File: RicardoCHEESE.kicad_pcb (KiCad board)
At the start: 4 copper layers, 54.7 x 68.3 mm, 143 parts, among them IC1 SiC437BED-T1-GE3, J1 RBUS, J2 USB_C_Receptacle_USB2.0, J3 Conn_Coaxial, J4 Conn_01x06_Pin, J5 Conn_01x06_Pin, J6 Conn_01x06_Pin, J7 Conn_01x06_Pin, J8 Conn_01x02_Male, U1 ESP32-S3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

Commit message: CHEESE routing finished V1
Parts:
- moved TP18 6.55 mm to (156.6, 97.4)
- moved C35 6.11 mm to (133.1, 97.2), turned to 180 degrees
- moved C9 4.71 mm to (124.9, 63.4), turned to 90 degrees
- moved C2 4.58 mm to (128.9, 63.4), turned to -90 degrees
- moved TP2 3.94 mm to (128.0, 65.9)
- moved C36 3.10 mm to (130.1, 94.8), turned to 90 degrees
- moved L2 1.91 mm to (126.2, 66.6), turned to 90 degrees
- moved TP9 1.46 mm to (139.9, 90.7)
- moved TP15 1.34 mm to (128.2, 97.8)
- moved Y1 1.05 mm to (126.9, 63.4), turned to 0 degrees
- moved C42 0.73 mm to (138.2, 94.2)
- moved R20 0.57 mm to (150.7, 102.7), turned to -90 degrees
- moved TP11 0.55 mm to (147.0, 121.3)
- moved R33 0.53 mm to (157.6, 107.7)
- moved R32 0.51 mm to (157.6, 109.7)
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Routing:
- net 5V_PWR: track 12.8 -> 109.4 mm, vias 0 -> 6
- net PA_EN: track 0.00 -> 70.1 mm, vias 0 -> 8
- net PHOTO0_TRIG: track 0.00 -> 62.8 mm, vias 0 -> 4
- net SEL2: track 0.00 -> 62.4 mm, vias 0 -> 2
- net PHOTO2_TRIG: track 0.00 -> 58.9 mm, vias 0 -> 2
- net CAMERA3_TRIG: track 0.00 -> 58.3 mm, vias 0 -> 4
- net CAMERA0_TRIG: track 0.00 -> 58.2 mm, vias 0 -> 2
- net SEL1: track 0.00 -> 54.1 mm, vias 0 -> 2
- net CAMERA2_TRIG: track 0.00 -> 52.5 mm, vias 0 -> 2
- net CAMERA1_TRIG: track 0.00 -> 52.1 mm, vias 0 -> 2
- net PHOTO3_TRIG: track 0.00 -> 50.3 mm, vias 0 -> 4
- net PHOTO1_TRIG: track 0.00 -> 44.3 mm, vias 0 -> 4
- net PWR_GOOD: track 0.00 -> 43.1 mm, vias 0 -> 4
- net CS0: track 0.00 -> 40.7 mm, vias 0 -> 4
- net CS1: track 0.00 -> 40.5 mm, vias 0 -> 6
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- added copper zone on F.Cu, net +3.3V
- added copper zone on F.Cu, net +3.3VA
- added copper zone on F.Cu, net 5V_PWR
- added copper zone on F.Cu, net Net-(IC1-SW_1)
- added copper zone on F.Cu, net Net-(IC1-VIN_1)
- added copper zone on F.Cu, net Net-(U6-RF_IN)

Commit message: Finished routing
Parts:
- moved TP7 19.0 mm to (154.5, 81.4)
- moved J1 10.3 mm to (162.8, 68.2), turned to -90 degrees
- moved TP8 10.1 mm to (146.3, 88.6)
- moved TP10 5.99 mm to (151.8, 87.1)
- moved TP9 4.12 mm to (143.4, 88.5)
- moved R3 2.84 mm to (152.6, 66.7), turned to 90 degrees
- moved 12VLED1 0.91 mm to (151.2, 66.7), turned to 90 degrees
- moved TP5 0.67 mm to (120.1, 76.4)
- moved C14 0.66 mm to (119.3, 64.5), turned to -90 degrees
- moved TP3 0.50 mm to (122.3, 77.3)
- moved R12 0.45 mm to (120.0, 78.9)
- moved R14 0.27 mm to (149.7, 83.2), turned to 90 degrees
- moved TP4 0.19 mm to (123.4, 83.2)
- moved D2 0.10 mm to (123.3, 80.5), turned to -90 degrees
- turned C13 to 90 degrees
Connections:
- D2 pad 2: VBUS -> /Data-
- D2 pad 3: /Data- -> /Data+
- D2 pad 4: /Data+ -> VBUS
- U1 pad 30: unconnected-(U1-SPIHD/GPIO27-Pad30) -> /CAN_RX
- U1 pad 42: unconnected-(U1-GPIO37-Pad42) -> /CAN_TX
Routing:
- net VBUS: track 0.00 -> 54.4 mm, vias 0 -> 4
- net /Data+: track 0.00 -> 21.5 mm
- net /Data-: track 5.93 -> 19.8 mm
- net +3.3V: track 10.8 -> 23.9 mm, vias 6 -> 16
- net RBUS_uC_V: track 3.18 -> 14.6 mm
- net /Power/BBIN: track 0.00 -> 9.23 mm
- net GND: track 15.7 -> 24.7 mm, vias 6 -> 9
- net /CHIP_PU: track 5.71 -> 14.4 mm, vias 0 -> 2
- net /CAN_RX: track 0.00 -> 8.26 mm, vias 0 -> 2
- net /CAN+: track 10.4 -> 18.5 mm
- net /CAN-: track 9.73 -> 17.5 mm
- net /CAN_TX: track 0.00 -> 7.70 mm
- net /Power/BBOUT: track 0.00 -> 7.14 mm
- net /BOOT: track 3.55 -> 10.5 mm, vias 0 -> 2
- net +12V: track 0.25 -> 5.07 mm
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- added copper zone on F.Cu, net /Power/BBOUT
- added copper zone on F.Cu, net /Power/FBIn
- added copper zone on F.Cu, net Net-(C8-Pad2)

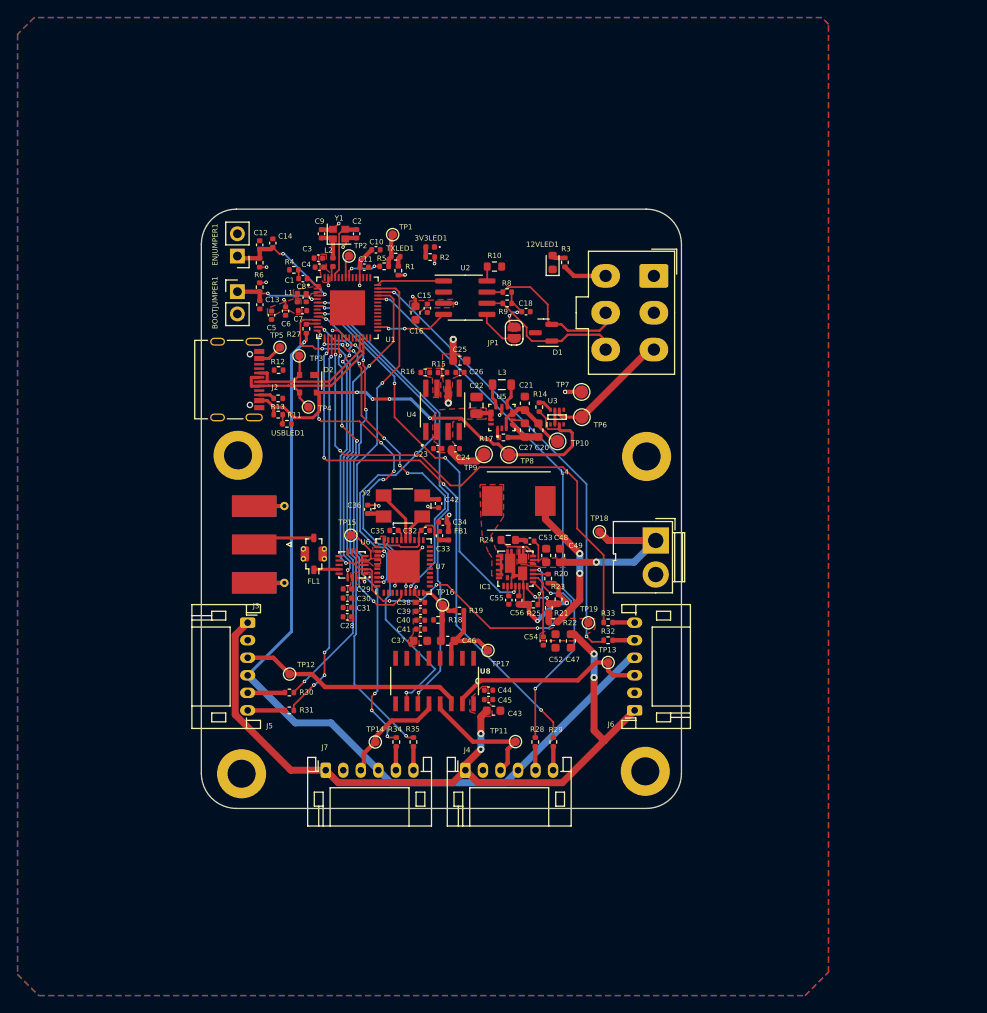
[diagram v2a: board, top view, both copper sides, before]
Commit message: radio side needs reviewing
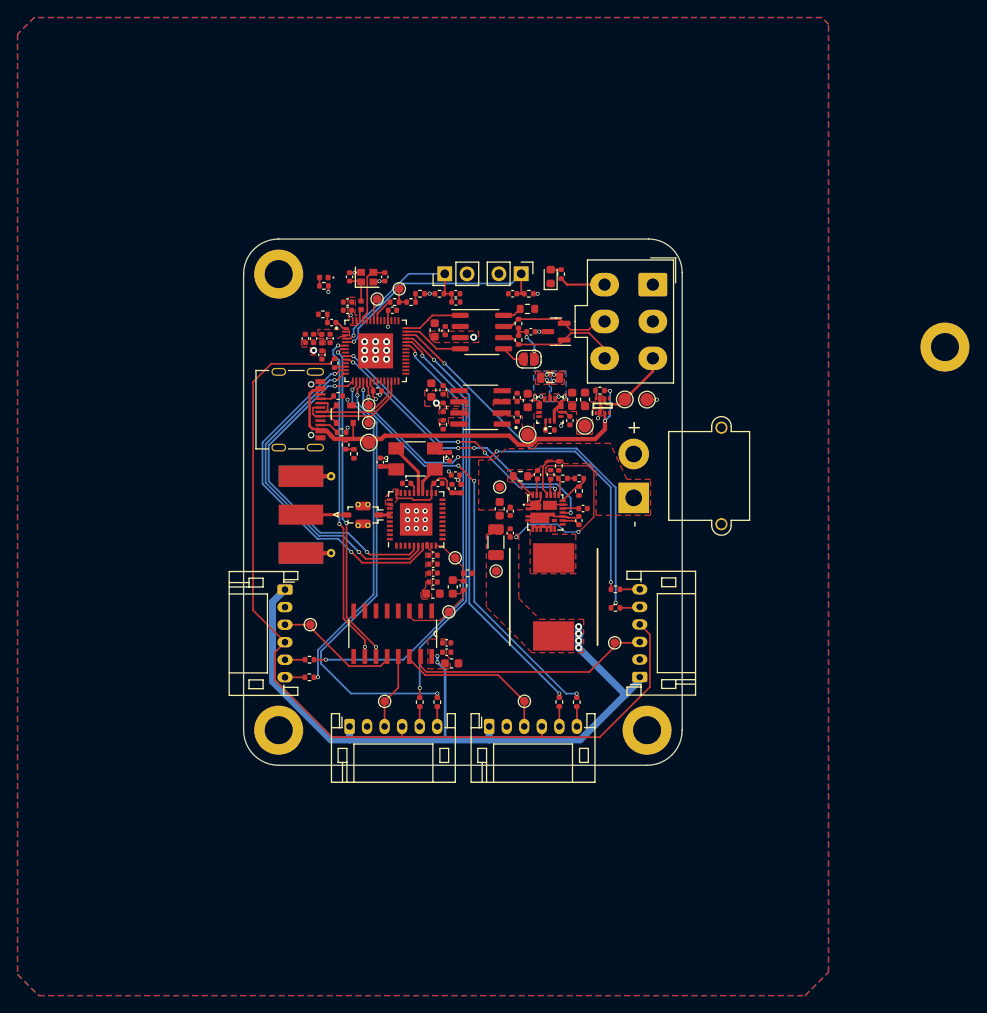
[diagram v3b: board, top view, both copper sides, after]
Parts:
- removed C28: 10u, Capacitor_SMD:C_0402_1005Metric
- removed C29, C30, C31: 100n, Capacitor_SMD:C_0402_1005Metric
- removed C47: 3u3, Capacitor_SMD:C_0603_1608Metric
- removed H2: MountingHole_Pad, MountingHole:MountingHole_3.2mm_M3_DIN965_Pad
- removed TP15, TP5: TestPoint, TestPoint:TestPoint_Pad_D1.0mm
- removed U6: SE5005L, fps:QFN300X300X100-16N
- added ?: , , F.Cu at (196.0, 76.3)
- C22: footprint Capacitor_SMD:C_0805_2012Metric -> Capacitor_SMD:C_0603_1608Metric
- C27: footprint Capacitor_SMD:C_0603_1608Metric -> Capacitor_SMD:C_0402_1005Metric
- C48: value 2u2 -> 10uF
- C49: value 1u5 -> 100nF; footprint Capacitor_SMD:C_0603_1608Metric -> Capacitor_SMD:C_0402_1005Metric
- C52: value 3u3 -> 47uF; footprint Capacitor_SMD:C_0603_1608Metric -> Capacitor_SMD:C_1206_3216Metric
- IC1: footprint fps:SiC437BEDT1GE3 -> iclr:SiC437BEDT1GE3
- J8: footprint Connector:JWT_A3963_1x02_P3.96mm_Vertical -> Connector_AMASS:AMASS_XT30PW-M_1x02_P2.50mm_Horizontal
- L4: value 11u -> 3.3uH; footprint Ricardo-CHEESE:IND_ASPI-0630HI-6R8M-T15 -> iclr:INDPM110100X540N
- R20: value 100k -> 51k
- R25: value 200k -> 100k
- U1: footprint fps:QFN40P700X700X90-57N -> iclr:QFN40P700X700X90-57N
- U3: footprint fps:SOTFL50P160X60-8N -> iclr:SOTFL50P160X60-8N
- U4: footprint fps:SOIC127P599X175-8N -> iclr:SOIC127P599X175-8N
- U5: footprint fps:CONV_MAX77827AEFD+T -> iclr:CONV_MAX77827AEFD+T
- U7: footprint Ricardo-CHEESE:RTC6705 -> iclr:RTC6705
- U8: footprint Ricardo-CHEESE:SOIC127P600X175-16N -> iclr:SOIC127P600X175-16N
- moved BOOTJUMPER1 32.4 mm to (147.7, 68.0), turned to -90 degrees
- moved R7 30.7 mm to (148.5, 70.2), turned to 180 degrees
- moved C13 28.8 mm to (146.7, 70.2), turned to 0 degrees
- moved ENJUMPER1 23.7 mm to (138.9, 68.0), turned to 90 degrees
- moved C12 23.0 mm to (140.2, 70.2), turned to 0 degrees
- moved C14 21.9 mm to (140.2, 71.2), turned to 180 degrees
- moved H1 21.2 mm to (120.0, 68.0)
- moved R6 20.8 mm to (138.3, 70.2), turned to 0 degrees
- moved R22 16.4 mm to (152.4, 91.3), turned to 0 degrees
- moved C10 16.1 mm to (131.2, 81.3)
- moved R25 16.1 mm to (151.9, 89.9), turned to 90 degrees
- moved TP8 16.0 mm to (130.3, 87.2), turned to -90 degrees
- moved R21 15.2 mm to (154.3, 91.3), turned to 0 degrees
- moved C52 13.2 mm to (144.8, 98.6), turned to -90 degrees
- moved C54 12.9 mm to (146.4, 97.5), turned to 90 degrees
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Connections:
- C56 pad 1: /Camera System/Camera Power Buck Converter/GNDA -> GND
- FL1 pad 1: /Camera System/RFOUT -> Net-(FL1-IN)
- IC1 pad 16: /Camera System/Camera Power Buck Converter/GNDA -> GND
- IC1 pad 19: PA_EN -> PWR_EN
- IC1 pad 25: /Camera System/Camera Power Buck Converter/GNDA -> GND
- R20 pad 2: /Camera System/Camera Power Buck Converter/GNDA -> GND
- R23 pad 2: /Camera System/Camera Power Buck Converter/GNDA -> GND
- R25 pad 1: /Camera System/Camera Power Buck Converter/GNDA -> GND
- U1 pad 10: PA_EN -> PWR_GOOD
- U1 pad 11: PA_PWR_DET -> unconnected-(U1-GPIO6/ADC1_CH5-Pad11)
- U1 pad 13: CS0 -> CS2
- U1 pad 15: CS2 -> CS0
- U1 pad 16: PHOTO0_TRIG -> PHOTO1_TRIG
- U1 pad 17: PHOTO1_TRIG -> PHOTO3_TRIG
- U1 pad 18: PHOTO2_TRIG -> PHOTO0_TRIG
- U1 pad 19: PHOTO3_TRIG -> PHOTO2_TRIG
- U1 pad 30: /CAN_RX -> unconnected-(U1-SPIHD/GPIO27-Pad30)
- U1 pad 37: unconnected-(U1-SPICLK_P/GPIO47-Pad37) -> CAMERA1_TRIG
- U1 pad 38: CAMERA0_TRIG -> CAMERA3_TRIG
- U1 pad 39: CAMERA1_TRIG -> CAMERA0_TRIG
- U1 pad 41: CAMERA3_TRIG -> /CAN_RX
- U1 pad 6: SEL1 -> SEL2
- U1 pad 7: SEL2 -> SEL1
- U1 pad 9: PWR_GOOD -> PWR_EN
- U3 pad 2: /Power/VoutDiode -> /Power/BBIN
- U3 pad 7: /Power/VoutDiode -> /Power/BBIN
- U7 pad 34: Net-(U6-RF_IN) -> Net-(FL1-IN)
- U7 pad 35: Net-(U6-RF_IN) -> Net-(FL1-IN)
- U8 pad 12: /Camera System/CAMERA3 -> /Camera System/CAMERA1
- U8 pad 13: /Camera System/CAMERA0 -> /Camera System/CAMERA3
- U8 pad 14: /Camera System/CAMERA1 -> /Camera System/CAMERA0
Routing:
- net PA_EN: track 70.1 -> 0.00 mm, vias 8 -> 0
- net PA_PWR_DET: track 36.5 -> 0.00 mm, vias 2 -> 0
- net PWR_EN: track 0.00 -> 31.0 mm, vias 0 -> 4
- net SEL2: track 62.8 -> 38.0 mm, vias 2 -> 3
- net Net-(IC1-VIN_1): track 18.8 -> 1.44 mm, vias 1 -> 0
- net SEL1: track 54.4 -> 37.5 mm, vias 2 -> 3
- net /BOOT: track 10.5 -> 27.0 mm, vias 2 -> 1
- net +3.3V: track 23.9 -> 9.09 mm, vias 16 -> 11
- net /Camera System/Camera Power Buck Converter/GNDA: track 14.6 -> 0.00 mm, vias 2 -> 0
- net GND: track 24.7 -> 10.4 mm, vias 9 -> 29
- net PHOTO0_TRIG: track 62.8 -> 49.2 mm
- net PHOTO2_TRIG: track 60.6 -> 47.1 mm, vias 2 -> 4
- net CAMERA0_TRIG: track 61.9 -> 48.6 mm
- net CAMERA3_TRIG: track 58.3 -> 46.0 mm, vias 4 -> 2
- net /Camera System/CAMERA1: track 25.7 -> 14.4 mm
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- added copper zone on F.Cu, net /Power/BBIN
- added copper zone on B.Cu, net /Power/LX1
- added copper zone on F.Cu, net /Power/LX1
- added copper zone on B.Cu, net /Power/LX2
- added copper zone on F.Cu, net /Power/LX2
- removed copper zone on F.Cu, net Net-(U6-RF_IN)
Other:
- board size 54.7 x 68.3 mm -> 50 x 60 mm
